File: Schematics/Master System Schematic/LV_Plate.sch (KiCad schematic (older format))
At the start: 3 parts

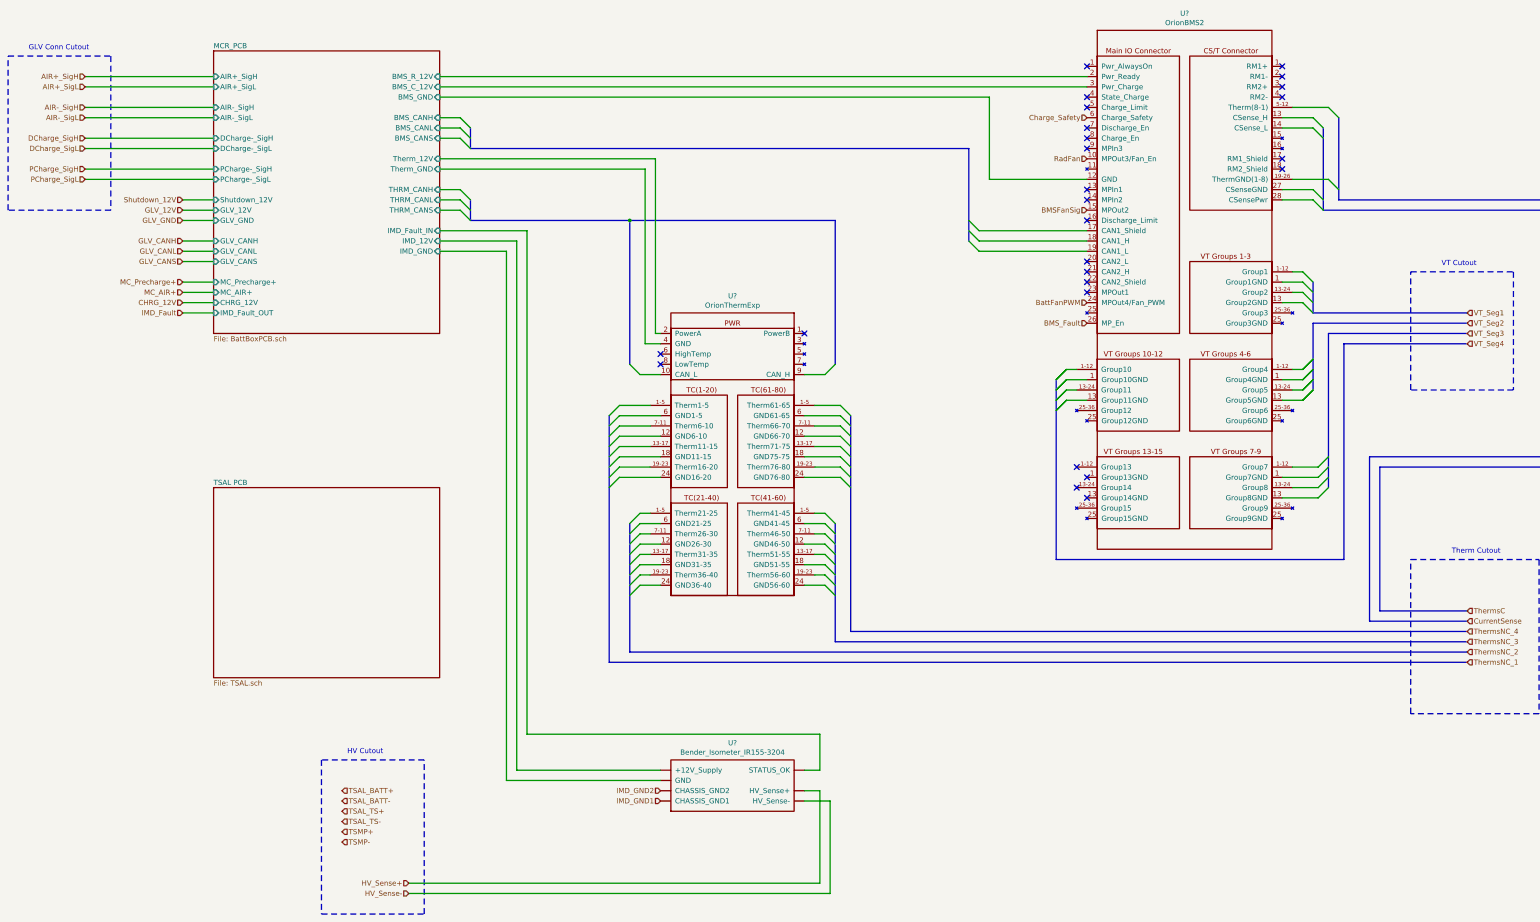
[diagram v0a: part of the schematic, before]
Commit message: Battery Box KiCAD Update (#103)
* LV Plate and VPM board

Verified and updated LV plate connections
Setup VPM board stand-in
Organized main battery box schematic

* Battbox and master update

- Fixed all connections within battbox and did some formatting
- Added all battbox connections to master

* Annotations complete

* VPM callout

Added call to view altium schematic for VPM boarrd

* TSAL call out

Redirect to altium for TSAL

* Dates and stuff

- Final annotations
- Updated title blocks

* Exported

Plotted full file

Co-authored-by: Zack Perry <zperry2002@gmail.com>
Co-authored-by: Zack Perry <60787475+ziptol@users.noreply.github.com>
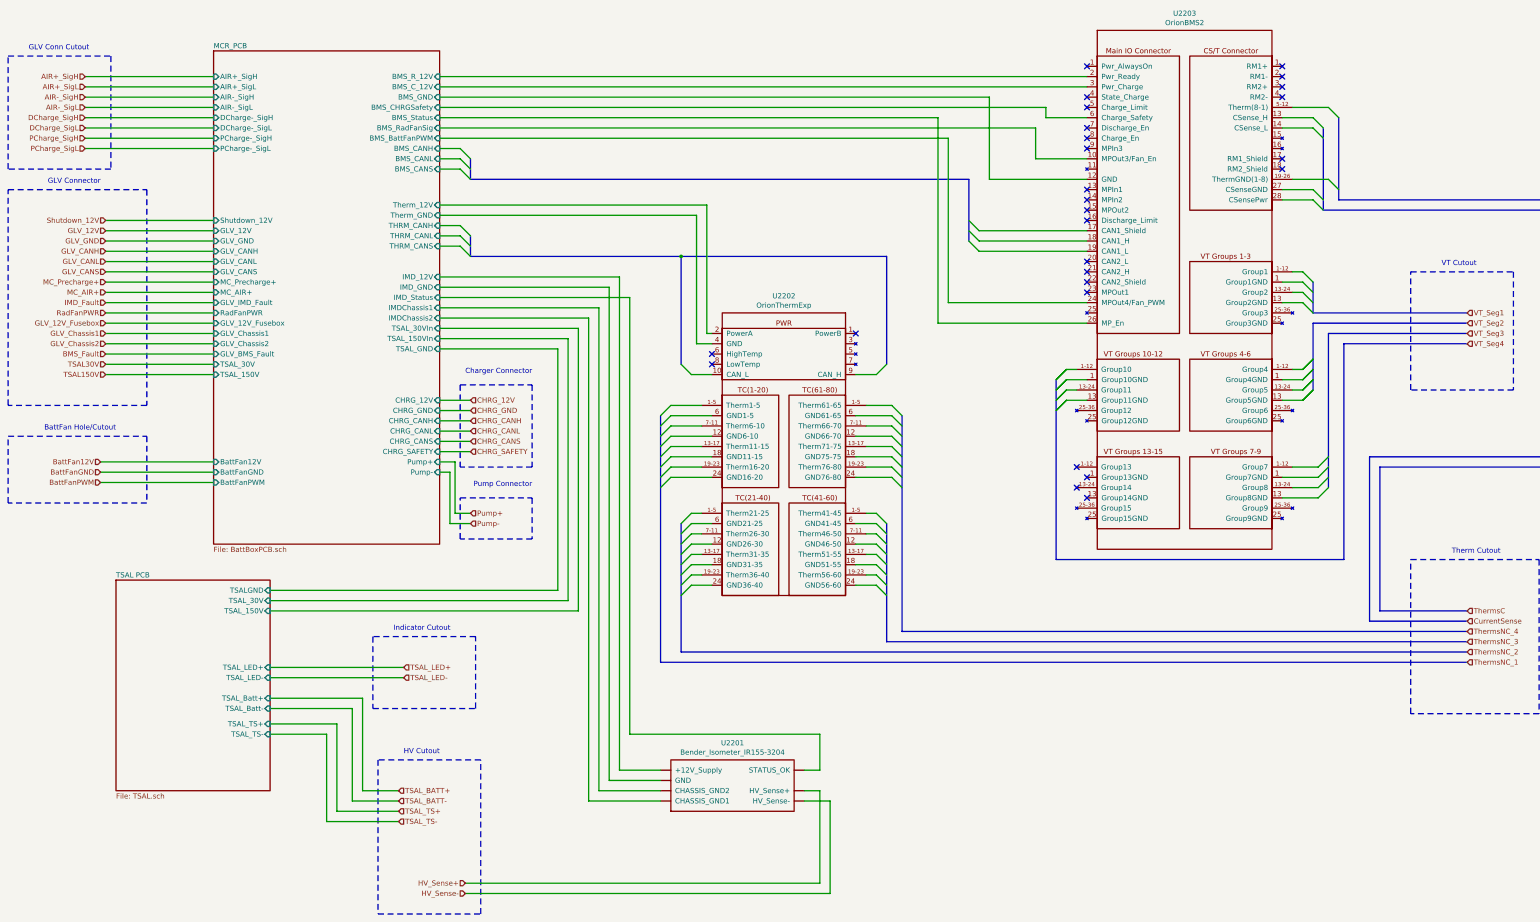
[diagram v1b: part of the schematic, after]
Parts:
- gave numbers to parts that had none: 3
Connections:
- net IMD_GND2 is gone; now on net MCR_PCB/IMD_Status: U2201.~ (STATUS_OK)
- net MCR_PCB/IMD_Fault_IN is gone; now on net MCR_PCB/IMD_Status: U2201.~ (STATUS_OK)
- net BMS_Fault: no longer U2203.26 (MP_En)
- net BattFanPWM: no longer U2203.24 (MPOut4/Fan_PWM)
- removed net BMSFanSig: U2203.15
- net Charge_Safety renamed MCR_PCB/BMS_CHRGSafety
- net IMD_GND1 renamed MCR_PCB/IMD_Status
- net RadFan renamed MCR_PCB/BMS_RadFanSig
- new net MCR_PCB/BMS_BattFanPWM: U2203.24 (MPOut4/Fan_PWM)
- new net MCR_PCB/BMS_Status: U2203.26 (MP_En)
- new net MCR_PCB/IMDChassis1: U2201.~ (STATUS_OK)
- new net MCR_PCB/IMDChassis2: U2201.~ (STATUS_OK)
- no-connect marks 26 -> 27
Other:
- note added: "BattFan Hole/Cutout"
- note added: "Charger Connector\n"
- note added: "GLV Connector"
- note added: "Indicator Cutout"
- note added: "Pump Connector\n"
- moved on the sheet: U2202
